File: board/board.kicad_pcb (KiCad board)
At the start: 2 copper layers, 21 x 61 mm, 9 parts, among them J1 007_ADC, J2 011_GPIO, J3 007_ADC, J4 007_ADC, J5 007_ADC, J6 007_ADC, U1 ADG707BRUZ-REEL7

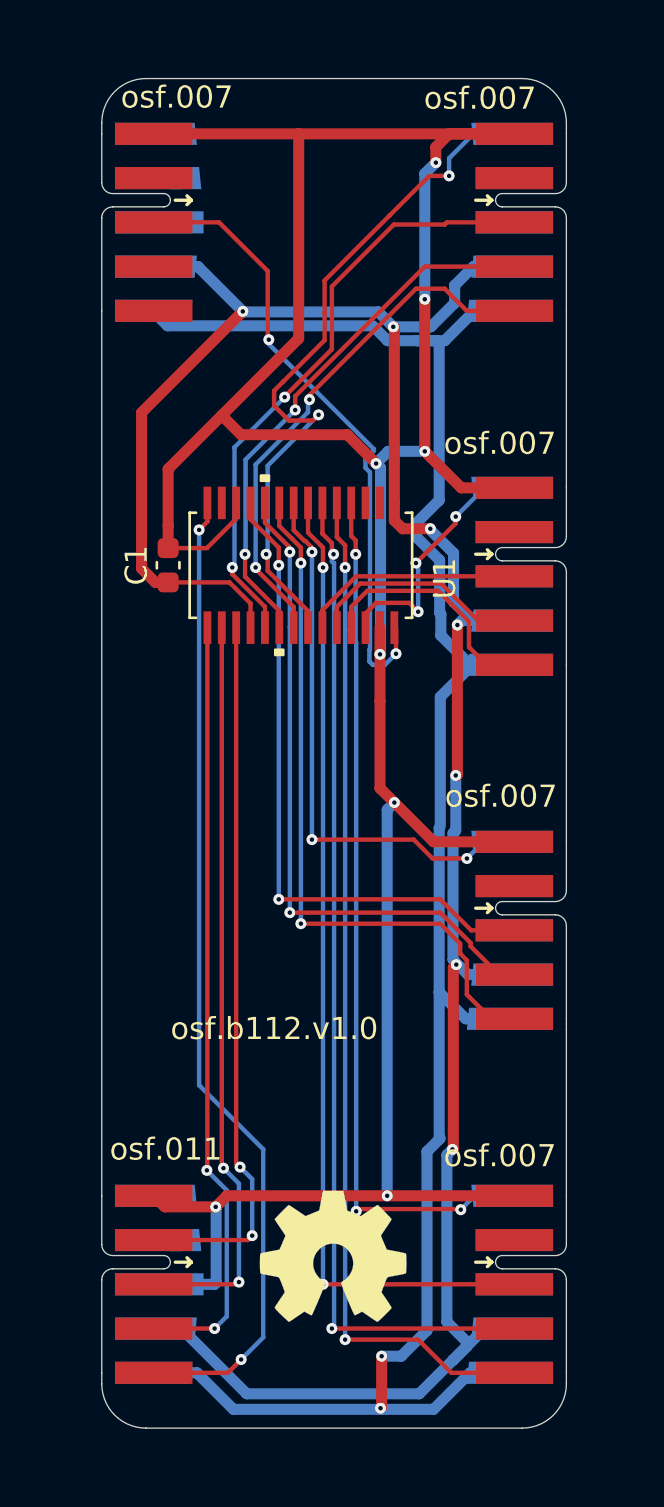
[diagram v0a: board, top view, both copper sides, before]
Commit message: fixed part number and added 3D model
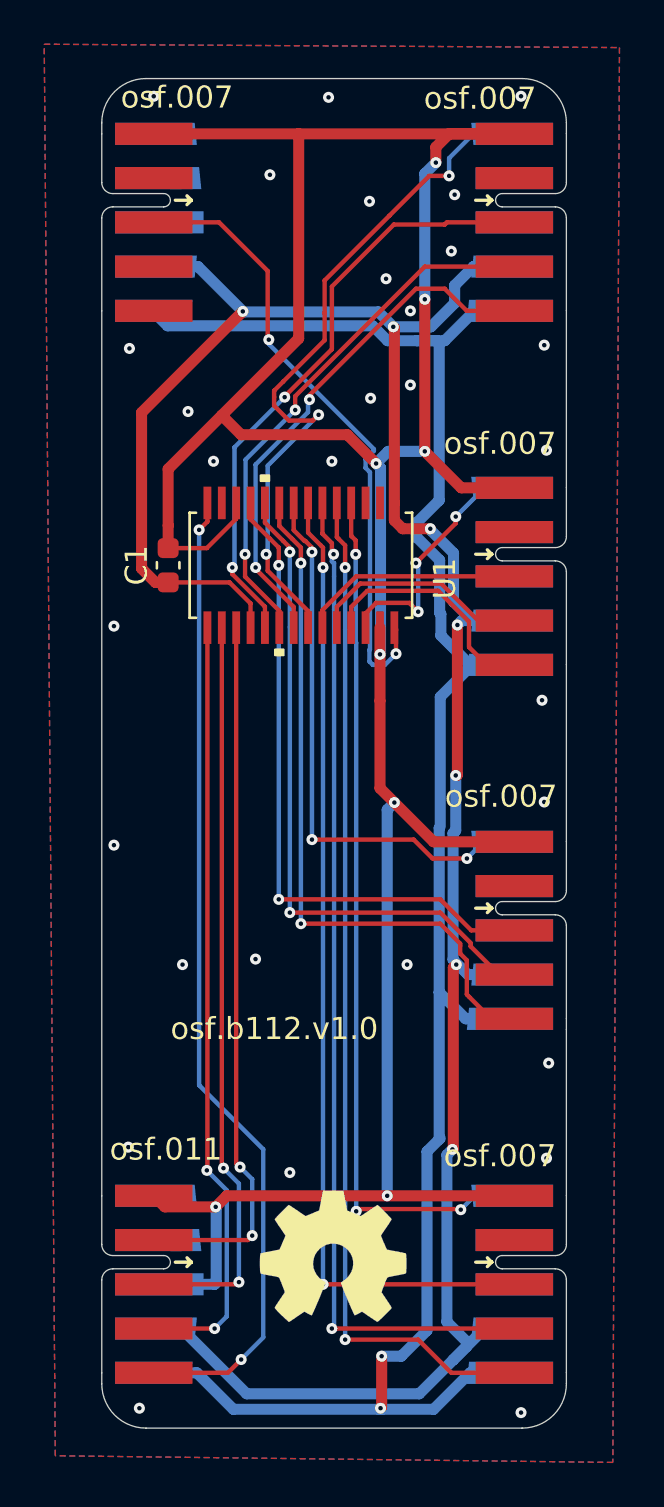
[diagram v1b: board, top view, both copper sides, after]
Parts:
- U1: value ADG707BRUZ-REEL7 -> ADG706BRUZ; footprint b112:ADG707BRUZ-REEL7 -> b112:ADG706BRUZ-REEL7
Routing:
- net GND: vias 8 -> 39
- added copper zone on B.Cu, net GND
- added copper zone on F.Cu, net GND
